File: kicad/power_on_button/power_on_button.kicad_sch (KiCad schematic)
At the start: 3 parts, among them J1 Conn_01x02_Pin, SW1 B3W-1000

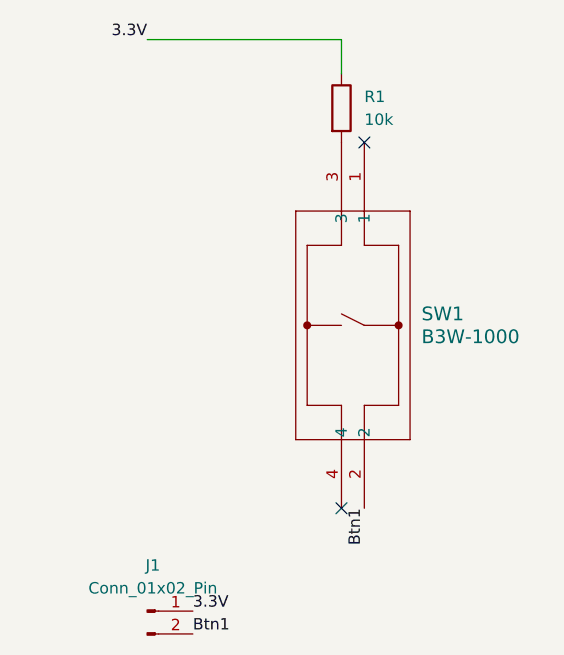
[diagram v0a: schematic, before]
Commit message: Add support for power on button (#8)
* add power button

* fix bug in power on button routing in hat

* update test_buttons.py script

* implement power off buttton in all fsm

* refactor display subsystem
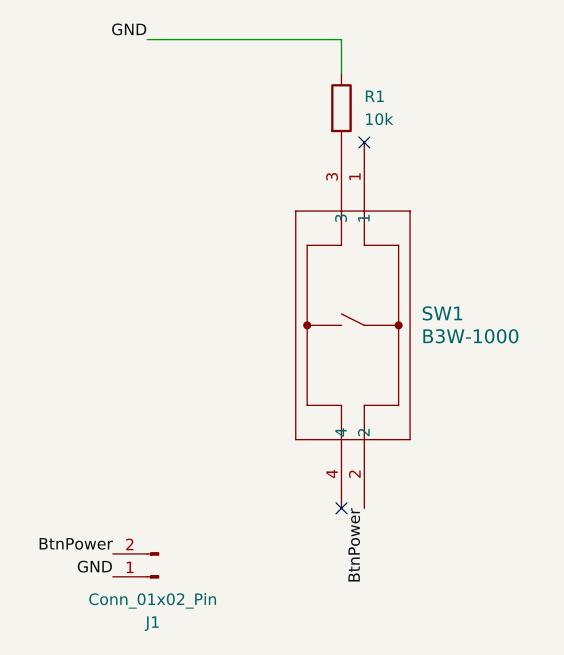
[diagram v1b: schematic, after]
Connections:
- net 3.3V renamed GND
- net Btn1 renamed BtnPower
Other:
- moved on the sheet: J1
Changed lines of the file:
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@@
 		)
 	)
-	(label "Btn1"
+	(label "BtnPower"
 		(at 63.5 85.09 270)
 		(effects
@@
 		)
 	)
-	(label "3.3V"
+	(label "GND"
 		(at 39.37 33.02 180)
 		(effects
@@
 		)
 	)
-	(label "3.3V"
-		(at 44.45 96.52 0)
+	(label "BtnPower"
+		(at 35.56 90.17 180)
 		(effects
 			(font
 				(size 1.27 1.27)
 			)
-			(justify left bottom)
+			(justify right bottom)
 		)
 	)
-	(label "Btn1"
-		(at 44.45 99.06 0)
+	(label "GND"
+		(at 35.56 92.71 180)
 		(effects
 			(font
 				(size 1.27 1.27)
 			)
-			(justify left bottom)
+			(justify right bottom)
 		)
 	)
@@
 	(symbol
 		(lib_id "Connector:Conn_01x02_Pin")
-		(at 39.37 96.52 0)
+		(at 40.64 92.71 180)
 		(unit 1)
 		(body_style 1)
@@
 		(fields_autoplaced yes)
 		(property "Reference" "J1"
-			(at 40.005 91.44 0)
+			(at 40.005 97.79 0)
 			(show_name no)
 			(do_not_autoplace no)
@@
 		)
 		(property "Value" "Conn_01x02_Pin"
-			(at 40.005 93.98 0)
+			(at 40.005 95.25 0)
 			(show_name no)
 			(do_not_autoplace no)
@@
 		)
 		(property "Footprint" "Connector_JST:JST_XH_S2B-XH-A_1x02_P2.50mm_Horizontal"
-			(at 39.37 96.52 0)
+			(at 40.64 92.71 0)
 			(hide yes)
 			(show_name no)
@@
 		)
 		(property "Datasheet" ""
-			(at 39.37 96.52 0)
+			(at 40.64 92.71 0)
 			(hide yes)
 			(show_name no)
@@
 		)
 		(property "Description" "Generic connector, single row, 01x02, script generated"
-			(at 39.37 96.52 0)
+			(at 40.64 92.71 0)
 			(hide yes)
 			(show_name no)
